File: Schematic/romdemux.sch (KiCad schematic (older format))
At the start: 17 parts, among them J1 Conn_01x01, J2 Conn_01x01, SW10 SW_Push, U10 28C256, U11 74LS154, U12 NE555, U13 74LS161

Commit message: Changed to horizontal resistors on PCB.
This resulted in only two vias, so that's nice.
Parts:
- R37, R38, R40, R41, R42: footprint Resistor_THT:R_Axial_DIN0204_L3.6mm_D1.6mm_P1.90mm_Vertical -> Resistor_THT:R_Axial_DIN0207_L6.3mm_D2.5mm_P7.62mm_Horizontal
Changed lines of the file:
@@
 F 0 "R38" H 7350 2800 50  0000 L CNN
 F 1 "1K" H 7350 2700 50  0000 L CNN
-F 2 "Resistor_THT:R_Axial_DIN0204_L3.6mm_D1.6mm_P1.90mm_Vertical" H 7250 2750 50  0001 C CNN
+F 2 "Resistor_THT:R_Axial_DIN0207_L6.3mm_D2.5mm_P7.62mm_Horizontal" H 7250 2750 50  0001 C CNN
 F 3 "" H 7250 2750 50  0001 C CNN
 	1    7250 2750
@@
 F 0 "R37" H 7000 2900 50  0000 L CNN
 F 1 "1K" H 7000 2800 50  0000 L CNN
-F 2 "Resistor_THT:R_Axial_DIN0204_L3.6mm_D1.6mm_P1.90mm_Vertical" H 6900 2850 50  0001 C CNN
+F 2 "Resistor_THT:R_Axial_DIN0207_L6.3mm_D2.5mm_P7.62mm_Horizontal" H 6900 2850 50  0001 C CNN
 F 3 "" H 6900 2850 50  0001 C CNN
 	1    6900 2850
@@
 F 0 "R40" H 5050 6850 50  0000 L CNN
 F 1 "1K" H 5050 6750 50  0000 L CNN
-F 2 "Resistor_THT:R_Axial_DIN0204_L3.6mm_D1.6mm_P1.90mm_Vertical" H 5250 6800 50  0001 C CNN
+F 2 "Resistor_THT:R_Axial_DIN0207_L6.3mm_D2.5mm_P7.62mm_Horizontal" H 5250 6800 50  0001 C CNN
 F 3 "" H 5250 6800 50  0001 C CNN
 	1    5250 6800
@@
 F 0 "R42" V 9004 3650 50  0000 C CNN
 F 1 "20K" V 9095 3650 50  0000 C CNN
-F 2 "Resistor_THT:R_Axial_DIN0204_L3.6mm_D1.6mm_P1.90mm_Vertical" H 9200 3650 50  0001 C CNN
+F 2 "Resistor_THT:R_Axial_DIN0207_L6.3mm_D2.5mm_P7.62mm_Horizontal" H 9200 3650 50  0001 C CNN
 F 3 "~" H 9200 3650 50  0001 C CNN
 	1    9200 3650
@@
 F 0 "R41" H 8591 4204 50  0000 R CNN
 F 1 "100K" H 8591 4295 50  0000 R CNN
-F 2 "Resistor_THT:R_Axial_DIN0204_L3.6mm_D1.6mm_P1.90mm_Vertical" H 8650 4250 50  0001 C CNN
+F 2 "Resistor_THT:R_Axial_DIN0207_L6.3mm_D2.5mm_P7.62mm_Horizontal" H 8650 4250 50  0001 C CNN
 F 3 "~" H 8650 4250 50  0001 C CNN
 	1    8650 4250

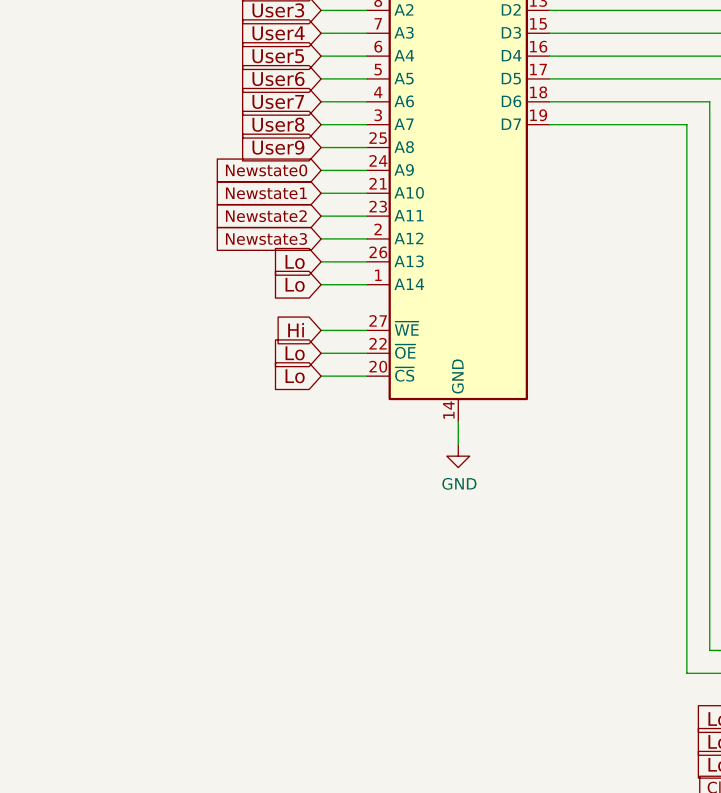
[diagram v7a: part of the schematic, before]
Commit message: Thanks to Ken Yap, I modified the project to optionally allow the board to move first.
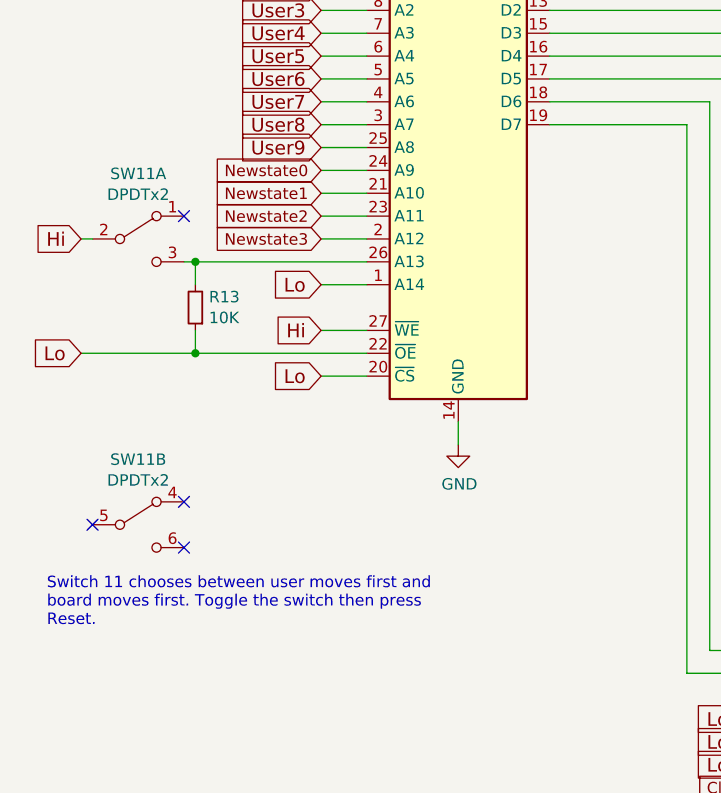
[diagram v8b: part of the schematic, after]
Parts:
- added R13: 10K, Resistor_THT:R_Axial_DIN0207_L6.3mm_D2.5mm_P7.62mm_Horizontal, symbol Device:R_Small
- added SW11: DPDTx2, Package_DIP:DIP-6_W7.62mm, symbol Switch:SW_DPDT_x2
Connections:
- net GND: now also R13.1; no longer U10.26 (A13)
- net VCC: now also SW11.2 (B)
- new net: R13.2, SW11.3 (C), U10.26 (A13)
- no-connect marks 7 -> 11
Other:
- note added: "Switch 11 chooses between user moves first and\nboard moves first. Toggle the switch then press\nReset."
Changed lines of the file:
@@
 	6900 3250 6900 3350
 Connection ~ 6900 3350
-Text GLabel 1750 2550 0    60   Input ~ 0
-Lo
 Text GLabel 1750 2650 0    60   Input ~ 0
 Lo
@@
 User9
 Wire Wire Line
-	1750 2950 1950 2950
+	700  2950 1200 2950
 Wire Wire Line
 	1750 2850 1950 2850
 Wire Wire Line
 	1750 2650 1950 2650
-Wire Wire Line
-	1750 2550 1950 2550
 Wire Wire Line
 	1750 2450 1950 2450
@@
 Text GLabel 1750 2450 0    50   Input ~ 0
 Newstate3
-Text GLabel 1750 2950 0    60   Input ~ 0
+Text GLabel 700  2950 0    60   Input ~ 0
 Lo
 Text GLabel 1750 3050 0    60   Input ~ 0
@@
 Text GLabel 6800 3350 0    60   Input ~ 0
 Hi
+$Comp
+L Switch:SW_DPDT_x2 SW11
+U 1 1 5D0F1A64
+P 950 2450
+F 0 "SW11" H 950 2735 50  0000 C CNN
+F 1 "DPDTx2" H 950 2644 50  0000 C CNN
+F 2 "Package_DIP:DIP-6_W7.62mm" H 950 2450 50  0001 C CNN
+F 3 "~" H 950 2450 50  0001 C CNN
+	1    950  2450
+	1    0    0    -1
+$EndComp
+NoConn ~ 1150 2350
+Wire Wire Line
+	1150 2550 1200 2550
+$Comp
+L Device:R_Small R13
+U 1 1 5D0FFD2D
+P 1200 2750
+F 0 "R13" H 1141 2704 50  0000 R CNN
+F 1 "10K" H 1141 2795 50  0000 R CNN
+F 2 "Resistor_THT:R_Axial_DIN0207_L6.3mm_D2.5mm_P7.62mm_Horizontal" H 1200 2750 50  0001 C CNN
+F 3 "~" H 1200 2750 50  0001 C CNN
+	1    1200 2750
+	-1   0    0    1
+$EndComp
+Wire Wire Line
+	1200 2850 1200 2950
+Connection ~ 1200 2950
+Wire Wire Line
+	1200 2950 1950 2950
+Wire Wire Line
+	1200 2550 1200 2650
+Connection ~ 1200 2550
+Wire Wire Line
+	1200 2550 1950 2550
+Text GLabel 700  2450 0    60   Input ~ 0
+Hi
+Wire Wire Line
+	700  2450 750  2450
+$Comp
+L Switch:SW_DPDT_x2 SW11
+U 2 1 5D118BBD
+P 950 3700
+F 0 "SW11" H 950 3985 50  0000 C CNN
+F 1 "DPDTx2" H 950 3894 50  0000 C CNN
+F 2 "Package_DIP:DIP-6_W7.62mm" H 950 3700 50  0001 C CNN
+F 3 "~" H 950 3700 50  0001 C CNN
+	2    950  3700
+	1    0    0    -1
+$EndComp
+NoConn ~ 1150 3600
+NoConn ~ 1150 3800
+NoConn ~ 750  3700
+Text Notes 550  4150 0    50   ~ 0
+Switch 11 chooses between user moves first and\nboard moves first. Toggle the switch then press\nReset.
 $EndSCHEMATC
